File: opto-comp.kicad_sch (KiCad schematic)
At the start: 99 parts, among them J1 CALIB_A, J2 INPUT_JACK, J3 OUTPUT_JACK, J4 POWER_CONN, J5 BYPASS_NOISE_FILTER, J6 CALIB_B, Q1 2SC1815, Q2 2SC1815, Q3 2SC1815, SW1 SW_DPDT_x2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

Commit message: fix LCR pattern, add credit
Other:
- company: meso.tokyo -> MST/mesotokyo
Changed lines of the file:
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@@
     (title "OPTO COMPRESSOR")
     (date "2024-01-07")
-    (rev "1.0.0")
-    (company "meso.tokyo")
+    (rev "1.0.1")
+    (company "MST/mesotokyo")
+    (comment 1 "https://meso.tokyo/")
   )
   (junction (at 207.01 133.35) (diameter 0) (color 0 0 0 0)

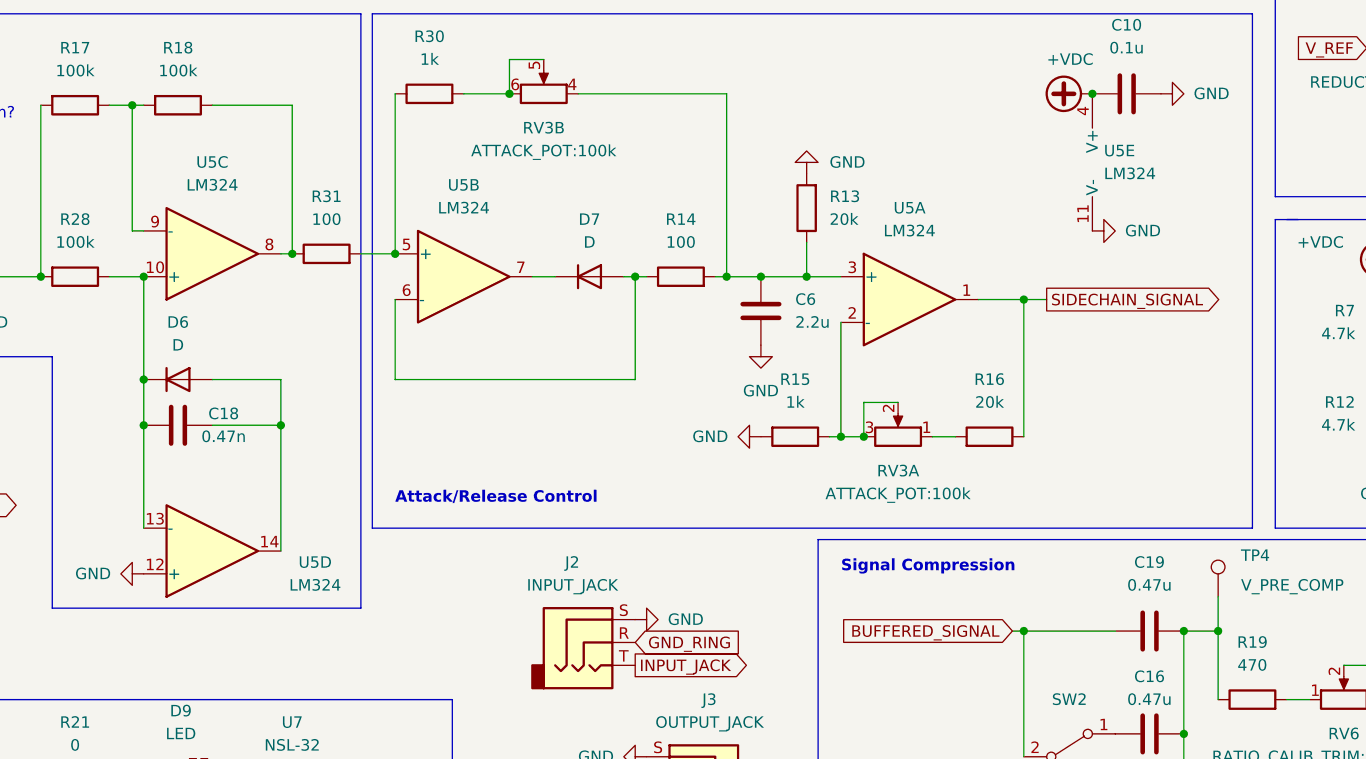
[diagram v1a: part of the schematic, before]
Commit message: Replace LM324 to NJM2902N
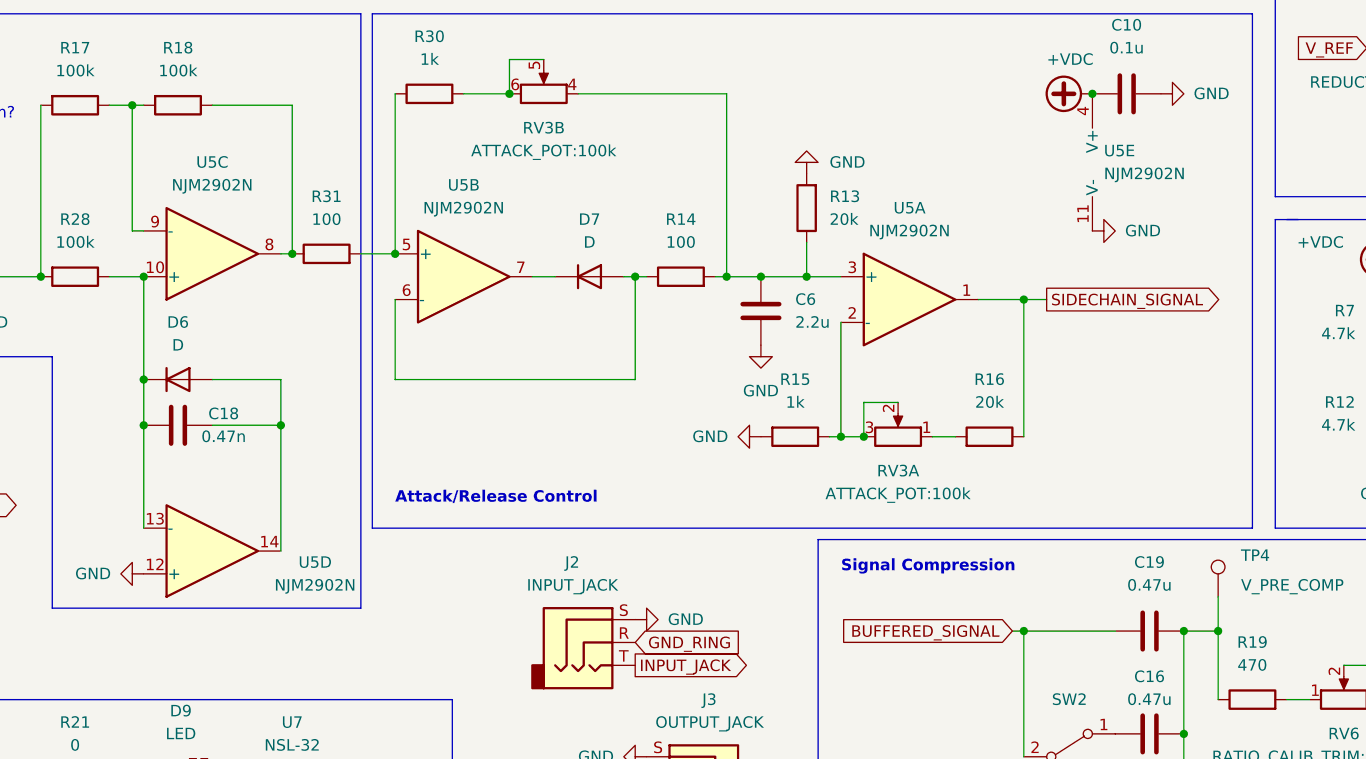
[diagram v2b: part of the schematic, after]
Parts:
- U5: value LM324 -> NJM2902N
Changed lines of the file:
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@@
     (in_bom yes) (on_board yes) (fields_autoplaced)
     (property "Reference" "U5" (id 0) (at 152.4 82.55 0))
-    (property "Value" "LM324" (id 1) (at 152.4 85.09 0))
+    (property "Value" "NJM2902N" (id 1) (at 152.4 85.09 0))
     (property "Footprint" "Package_DIP:DIP-14_W7.62mm_Socket" (id 2) (at 151.13 90.17 0)
       (effects (font (size 1.27 1.27)) hide)
@@
     (in_bom yes) (on_board yes)
     (property "Reference" "U5" (id 0) (at 86.36 121.92 0))
-    (property "Value" "LM324" (id 1) (at 86.36 124.46 0))
+    (property "Value" "NJM2902N" (id 1) (at 86.36 124.46 0))
     (property "Footprint" "Package_DIP:DIP-14_W7.62mm_Socket" (id 2) (at 73.66 123.19 0)
       (effects (font (size 1.27 1.27)) hide)
@@
     (in_bom yes) (on_board yes) (fields_autoplaced)
     (property "Reference" "U5" (id 0) (at 102.87 80.01 0))
-    (property "Value" "LM324" (id 1) (at 102.87 82.55 0))
+    (property "Value" "NJM2902N" (id 1) (at 102.87 82.55 0))
     (property "Footprint" "Package_DIP:DIP-14_W7.62mm_Socket" (id 2) (at 101.6 87.63 0)
       (effects (font (size 1.27 1.27)) hide)
@@
     (in_bom yes) (on_board yes) (fields_autoplaced)
     (property "Reference" "U5" (id 0) (at 74.93 77.47 0))
-    (property "Value" "LM324" (id 1) (at 74.93 80.01 0))
+    (property "Value" "NJM2902N" (id 1) (at 74.93 80.01 0))
     (property "Footprint" "Package_DIP:DIP-14_W7.62mm_Socket" (id 2) (at 73.66 90.17 0)
       (effects (font (size 1.27 1.27)) hide)
@@
       (effects (font (size 1.27 1.27)) (justify left))
     )
-    (property "Value" "LM324" (id 1) (at 173.99 78.7399 0)
+    (property "Value" "NJM2902N" (id 1) (at 173.99 78.7399 0)
       (effects (font (size 1.27 1.27)) (justify left))
     )
@@
     )
     (path "/09615e57-b282-4814-9ac2-5e912cc35208"
-      (reference "U5") (unit 1) (value "LM324") (footprint "Package_DIP:DIP-14_W7.62mm_Socket")
+      (reference "U5") (unit 1) (value "NJM2902N") (footprint "Package_DIP:DIP-14_W7.62mm_Socket")
     )
     (path "/befe503f-de8a-48c9-94b4-b995dc54ae6f"
-      (reference "U5") (unit 2) (value "LM324") (footprint "Package_DIP:DIP-14_W7.62mm_Socket")
+      (reference "U5") (unit 2) (value "NJM2902N") (footprint "Package_DIP:DIP-14_W7.62mm_Socket")
     )
     (path "/ea0dd20d-e625-402c-93eb-4e2da7ded819"
-      (reference "U5") (unit 3) (value "LM324") (footprint "Package_DIP:DIP-14_W7.62mm_Socket")
+      (reference "U5") (unit 3) (value "NJM2902N") (footprint "Package_DIP:DIP-14_W7.62mm_Socket")
     )
     (path "/9b4768b8-1003-43f9-861d-fd974cbf29c4"
-      (reference "U5") (unit 4) (value "LM324") (footprint "Package_DIP:DIP-14_W7.62mm_Socket")
+      (reference "U5") (unit 4) (value "NJM2902N") (footprint "Package_DIP:DIP-14_W7.62mm_Socket")
     )
     (path "/fb949e42-6025-43bf-bdb7-6de11a3194fd"
-      (reference "U5") (unit 5) (value "LM324") (footprint "Package_DIP:DIP-14_W7.62mm_Socket")
+      (reference "U5") (unit 5) (value "NJM2902N") (footprint "Package_DIP:DIP-14_W7.62mm_Socket")
     )
     (path "/9a93c812-3b67-45ca-a513-d2268828ef43"
